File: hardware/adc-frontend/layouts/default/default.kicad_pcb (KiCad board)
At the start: 4 copper layers, 142.2 x 111.6 mm, 133 parts

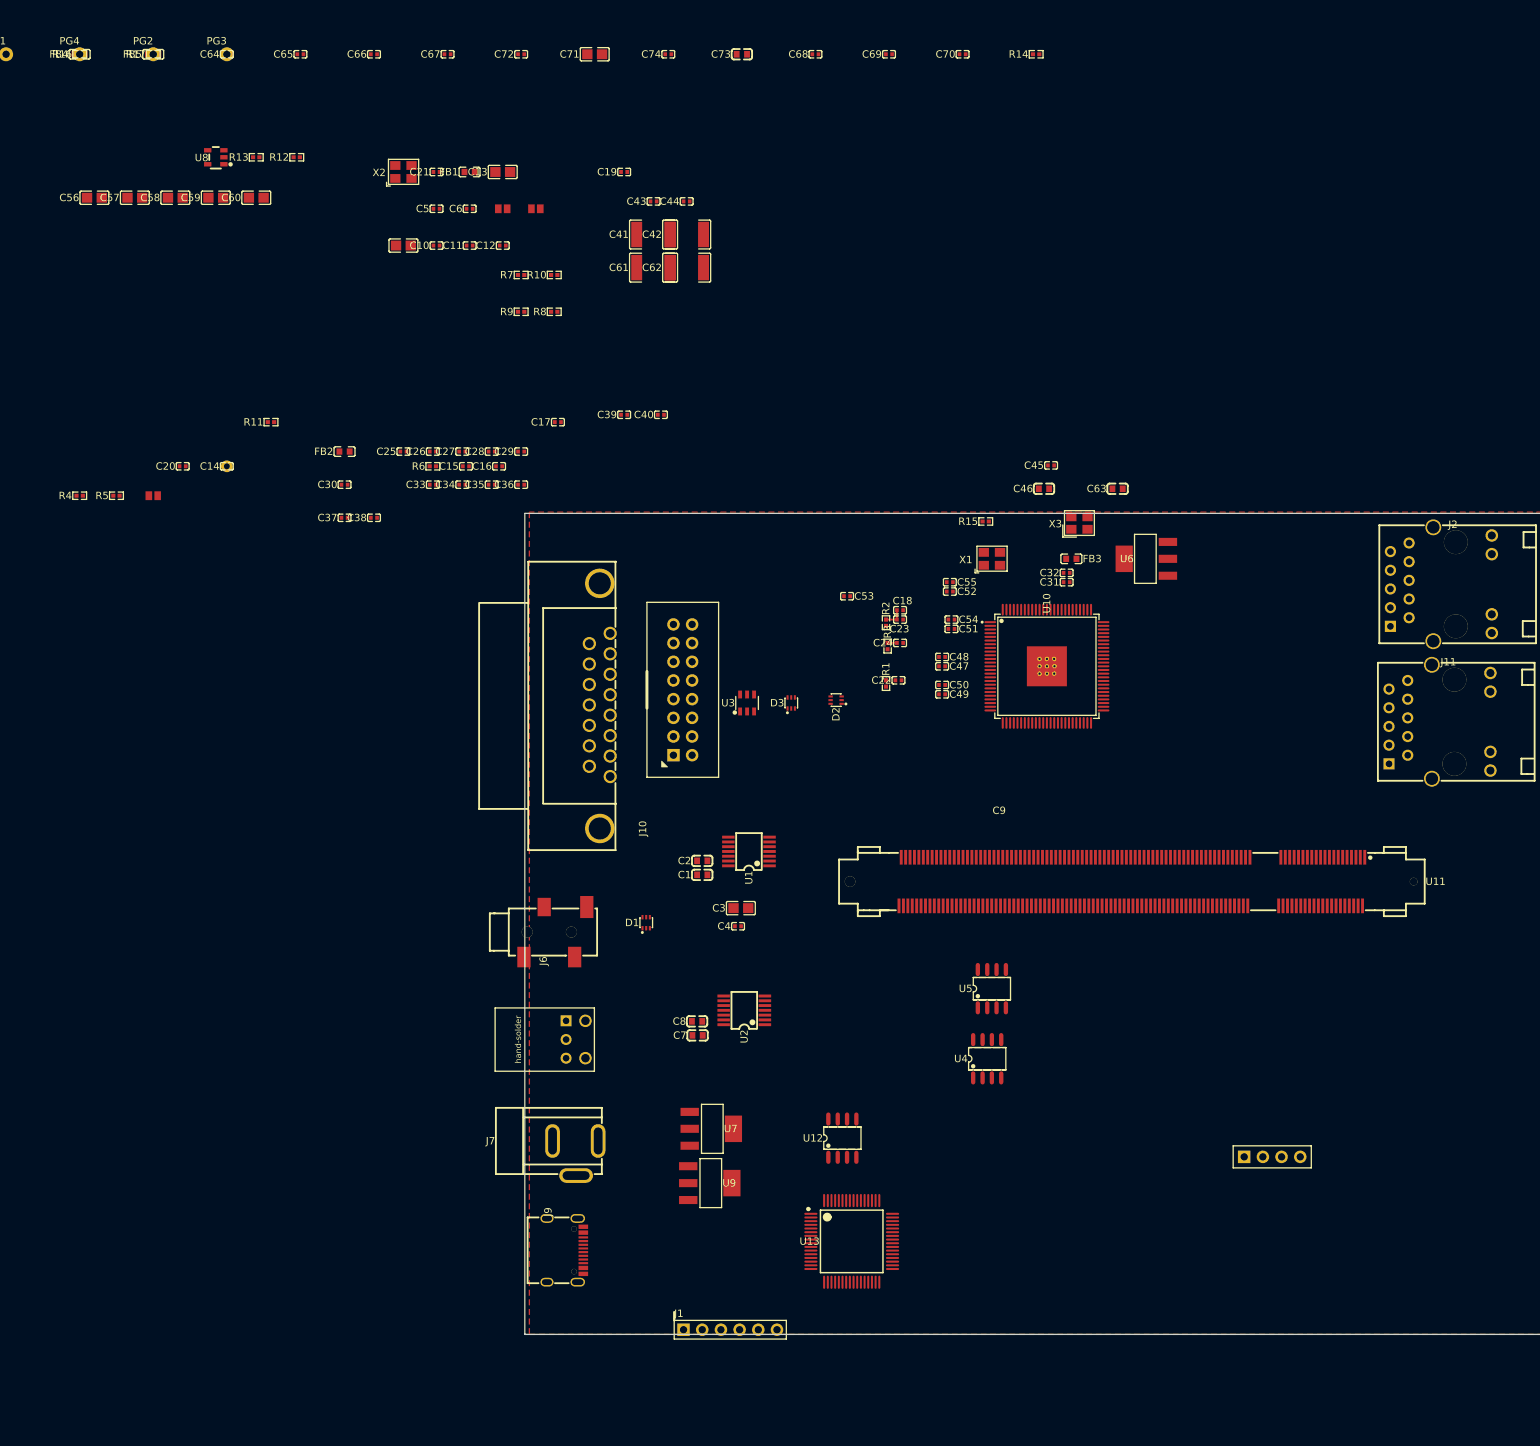
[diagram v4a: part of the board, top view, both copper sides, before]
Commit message: 映像バス: TVPビット順修正 + P2/P3再配置 + spdif移設
- Tvp7002定義のR/G/Bビット順をデータシート/シンボルに合わせて修正
  (若番ピン=MSB, pin29=B9…pin38=B0)。上位8bit[9:2]を正しくキャプチャ。
- 映像24bitをSO-DIMM昇順↔TVP物理降順の単調写像に整列(向かい合わせ配置で
  クロスなし配線)。B6-B9をP4後列→P3前列の連続run(pin117-123)へ移設。
  → ext基板でもP2(20)+P3で映像が完結。旧P4ボールE1/E4/H3/H5は空きに。
- spdifをpin109(E19)→P3後半pin125(C17)へ移設(映像ファンアウトを横切らない)。
  gatewareのspdifピン制約も同期(E19→C17)。ネット名をspdifに固定。
- sodimm_i5.atoにP3ボール(B20/B19/B18/A19/C17=pin117/119/121/123/125)追加。

Co-Authored-By: Claude Opus 4.8 (1M context) <noreply@anthropic.com>
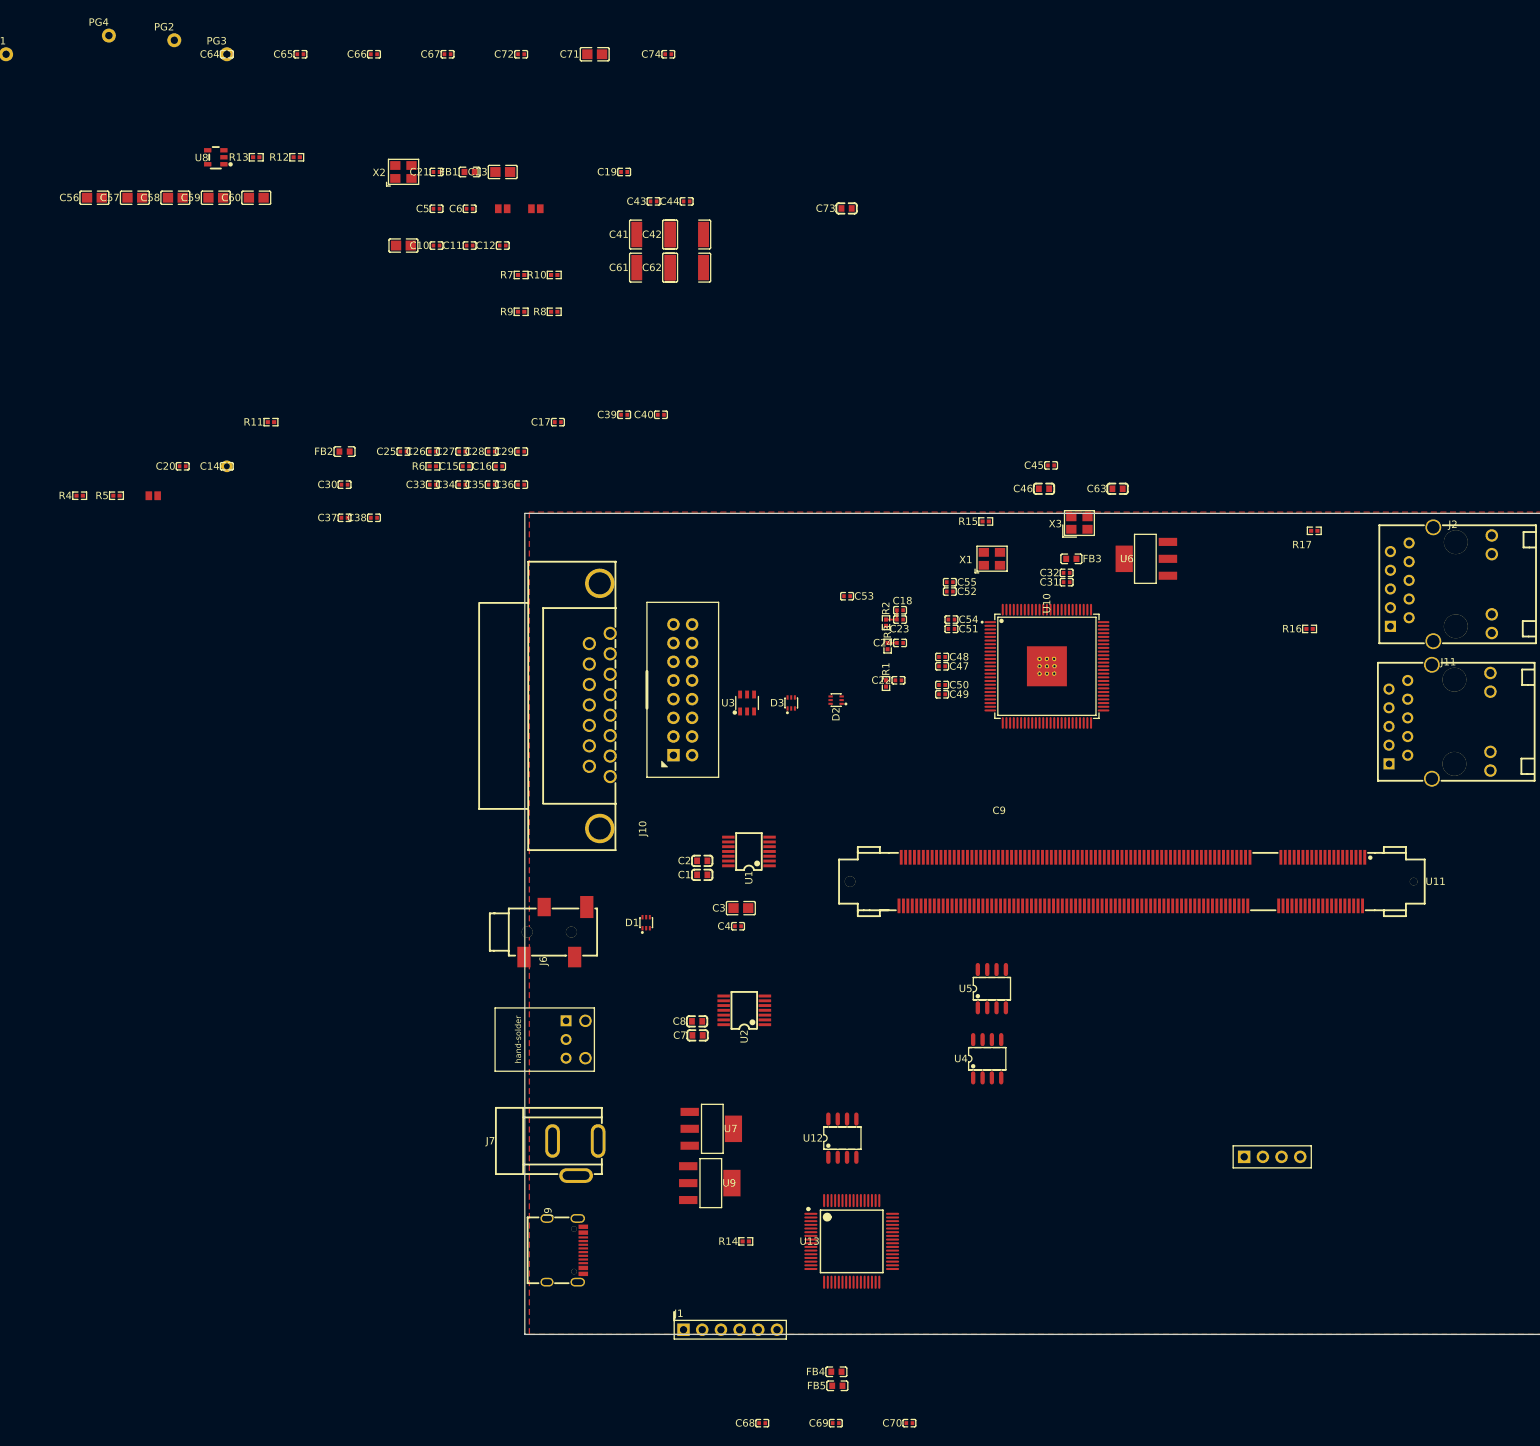
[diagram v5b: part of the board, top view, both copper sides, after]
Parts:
- moved FB4 206.5 mm to (112.8, 179.1)
- moved FB5 203.5 mm to (113.0, 181.0)
- moved C68 186.2 mm to (102.8, 186.1)
- moved C69 186.2 mm to (112.8, 186.1)
- moved C70 186.2 mm to (122.8, 186.1)
- moved R16 184.5 mm to (177.2, 78.1)
- moved R17 170.6 mm to (177.8, 64.8)
- moved R14 166.1 mm to (100.5, 161.3)
- moved C73 25.3 mm to (114.2, 21.0)
- moved PG4 4.71 mm to (14.0, -2.54)
- moved PG2 3.44 mm to (22.9, -1.91)
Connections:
- J8 pad 1: out -> spdif
- U10 pad 29: tvp-29 -> vd_b9
- U10 pad 30: tvp-30 -> vd_b8
- U10 pad 31: vd_b2 -> vd_b7
- U10 pad 32: vd_b3 -> vd_b6
- U10 pad 33: vd_b4 -> vd_b5
- U10 pad 34: vd_b5 -> vd_b4
- U10 pad 35: vd_b6 -> vd_b3
- U10 pad 36: vd_b7 -> vd_b2
- U10 pad 37: vd_b8 -> 37
- U10 pad 38: vd_b9 -> 38
- U10 pad 43: tvp-43 -> vd_g9
- U10 pad 44: tvp-44 -> vd_g8
- U10 pad 45: vd_g2 -> vd_g7
- U10 pad 46: vd_g3 -> vd_g6
- U10 pad 47: vd_g4 -> vd_g5
- U10 pad 48: vd_g5 -> vd_g4
- U10 pad 49: vd_g6 -> vd_g3
- U10 pad 50: vd_g7 -> vd_g2
- U10 pad 51: vd_g8 -> 51
- U10 pad 52: vd_g9 -> tvp-52
- U10 pad 55: tvp-55 -> vd_r9
- U10 pad 56: 56 -> vd_r8
- U10 pad 57: vd_r2 -> vd_r7
- U10 pad 58: vd_r3 -> vd_r6
- U10 pad 59: vd_r4 -> vd_r5
- U10 pad 61: vd_r5 -> vd_r4
- U10 pad 62: vd_r6 -> vd_r3
- U10 pad 63: vd_r7 -> vd_r2
- U10 pad 64: vd_r8 -> 64
- U10 pad 65: vd_r9 -> 65
- U11 pad 109: out -> 109
- U11 pad 117: (no net) -> vd_b6
- U11 pad 119: (no net) -> vd_b7
- U11 pad 121: (no net) -> vd_b8
- U11 pad 123: (no net) -> vd_b9
- U11 pad 125: (no net) -> spdif
- U11 pad 128: vd_b4 -> 128
- U11 pad 136: vd_b3 -> 136
- U11 pad 140: vd_b2 -> 140
- U11 pad 153: vd_b5 -> 153
- U11 pad 41: vd_b7 -> vd_r2
- U11 pad 49: vd_b6 -> vd_r3
- U11 pad 51: vd_b9 -> vd_r4
- U11 pad 57: vd_b8 -> vd_r5
- U11 pad 59: vd_g3 -> vd_r6
- U11 pad 61: vd_g2 -> vd_r7
- U11 pad 63: vd_g5 -> vd_r8
- U11 pad 65: vd_g4 -> vd_r9
- U11 pad 67: vd_g7 -> vd_g2
- U11 pad 69: vd_g6 -> vd_g3
- U11 pad 71: vd_g9 -> vd_g4
- U11 pad 73: vd_g8 -> vd_g5
- U11 pad 75: vd_r3 -> vd_g6
- U11 pad 77: vd_r2 -> vd_g7
- U11 pad 79: vd_r5 -> vd_g8
- U11 pad 81: vd_r4 -> vd_g9
- U11 pad 83: vd_r7 -> vd_b2
- U11 pad 85: vd_r6 -> vd_b3
- U11 pad 89: vd_r9 -> vd_b4
- U11 pad 95: vd_r8 -> vd_b5

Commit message: ETH1 LED追加 + SO-DIMMピン対応表(HTML)
- EthernetPort: ETH1(jack2)の緑/黄LED駆動を追加。P6でLED4本を連続配置
  (ETH2=io_r1/io_t1, ETH1=io_u1/io_y2)。UARTはio_w1/io_v1へ後送り。
  LEDネット名を eth2_led_g/y, eth1_led_g/y に固定。
- docs/sodimm-pinmap.html: SO-DIMM 200P全ピン対応表(左=奇数/右=偶数、
  FPGAボール・extヘッダ&ピン番号・ext機能・当基板割当、キー切り欠き表示)。
  典拠 wuxx README + ext-board pinout図 + litex platform。

Co-Authored-By: Claude Opus 4.8 (1M context) <noreply@anthropic.com>
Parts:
- added R18: {ℝ+}Ω, UNI_ROYAL_0402WGF2200TCE:R0402, F.Cu at (0.00, 0.00)
- added R19: {ℝ+}Ω, UNI_ROYAL_0402WGF2200TCE:R0402, F.Cu at (10.0, 0.00)
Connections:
- net led_g_drive renamed eth2_led_g
- net led_y_drive renamed eth2_led_y
- J11 pad 11: eth.jack2-led_g_a -> eth-led_g_a
- J11 pad 12: led_g_k -> gnd
- J11 pad 13: led_y_k -> gnd
- J11 pad 14: eth.jack2-led_y_a -> eth-led_y_a
- U11 pad 46: uart_txd -> eth1_led_g
- U11 pad 48: uart_rxd -> eth1_led_y
- U11 pad 50: (no net) -> uart_txd
- U11 pad 52: (no net) -> uart_rxd

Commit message: SO-DIMMピン再配置: 映像をP2/P3集約 + I2C/音声整理 + DATACLKをPCLKピンへ
- P2: SDA/SCL/RESETB(41/49/51) + R2-R9(57-71) + G2-G9(73-89)。
- P3: B2-B9集中(99-127) + TVPタイミング。SO-DIMM昇順↔TVP降順の単調は維持。
- 音声をP4に集約整理: SPDIF=E4, MCLK=F1, BCK=F3, LRCK=G3, DOUT=H3/H4。
  gateware _audio_io のピン制約も同期。
- DATACLK: 指定のD3はPCLK非対応(prjtrellis iodb確認)のため、P3唯一の
  クロック対応ピン E2=PCLKC7_0(pin151)へ。SPDIFはsysオーバーサンプリング
  復号でPLL不要=E4通常GPIOで可。nextpnr実ビルドで配置配線とクロック網載りを検証。
- docs/sodimm-pinmap.html を新レイアウトへ更新。

Co-Authored-By: Claude Opus 4.8 (1M context) <noreply@anthropic.com>
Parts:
- moved R18 205.8 mm to (181.4, 97.2)
- moved R19 193.8 mm to (181.2, 90.8)
- moved PG1 5.12 mm to (4.45, -2.54)
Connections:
- U11 pad 111: (no net) -> vd_b3
- U11 pad 117: vd_b6 -> vd_b4
- U11 pad 119: vd_b7 -> vd_b5
- U11 pad 121: vd_b8 -> vd_b6
- U11 pad 123: vd_b9 -> vd_b7
- U11 pad 125: spdif -> vd_b8
- U11 pad 127: (no net) -> vd_b9
- U11 pad 128: 128 -> spdif
- U11 pad 129: (no net) -> 129
- U11 pad 131: (no net) -> sogout
- U11 pad 132: i2s_dout_dsub -> audio_bck
- U11 pad 133: (no net) -> hsout
- U11 pad 134: audio_bck -> audio_lrck
- U11 pad 135: (no net) -> vsout
- U11 pad 136: 136 -> i2s_dout_dsub
- U11 pad 137: (no net) -> fidout
- U11 pad 138: audio_lrck -> i2s_dout_line
- U11 pad 142: i2s_dout_line -> 142
- U11 pad 144: hsout -> 144
- U11 pad 146: sda -> 146
- U11 pad 148: sogout -> 148
- U11 pad 150: scl -> 150
- U11 pad 151: (no net) -> dataclk
- U11 pad 152: resetb -> 152
- U11 pad 154: vsout -> 154
- U11 pad 155: dataclk -> 155
- U11 pad 156: fidout -> 156
- U11 pad 41: vd_r2 -> sda
- U11 pad 49: vd_r3 -> scl
- U11 pad 51: vd_r4 -> resetb
- U11 pad 57: vd_r5 -> vd_r2
- U11 pad 59: vd_r6 -> vd_r3
- U11 pad 61: vd_r7 -> vd_r4
- U11 pad 63: vd_r8 -> vd_r5
- U11 pad 65: vd_r9 -> vd_r6
- U11 pad 67: vd_g2 -> vd_r7
- U11 pad 69: vd_g3 -> vd_r8
- U11 pad 71: vd_g4 -> vd_r9
- U11 pad 73: vd_g5 -> vd_g2
- U11 pad 75: vd_g6 -> vd_g3
- U11 pad 77: vd_g7 -> vd_g4
- U11 pad 79: vd_g8 -> vd_g5
- U11 pad 81: vd_g9 -> vd_g6
- U11 pad 83: vd_b2 -> vd_g7
- U11 pad 85: vd_b3 -> vd_g8
- U11 pad 89: vd_b4 -> vd_g9
- U11 pad 95: vd_b5 -> 95
- U11 pad 99: (no net) -> vd_b2
